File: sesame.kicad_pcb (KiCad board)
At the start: 2 copper layers, 344.4 x 130.9 mm, 166 parts, among them U1 ATmega32A-PU

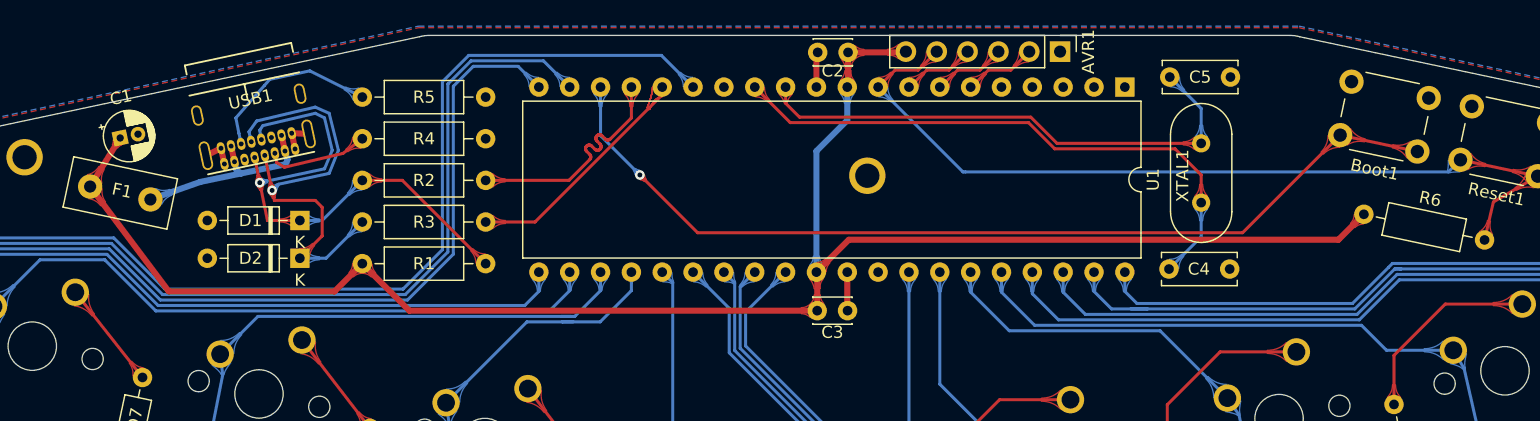
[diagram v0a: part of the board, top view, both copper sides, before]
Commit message: Change to Mini USB
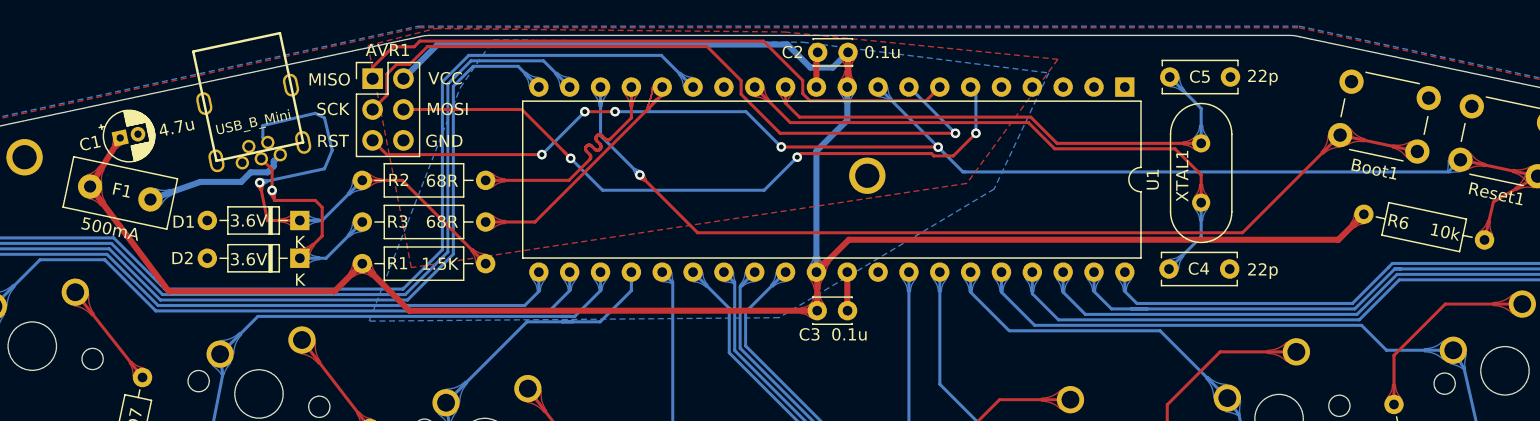
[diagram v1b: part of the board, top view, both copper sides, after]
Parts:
- removed R4, R5: 5.1K, Resistor_THT:R_Axial_DIN0207_L6.3mm_D2.5mm_P10.16mm_Horizontal
- AVR1: value Conn_01x06 -> Conn_02x03_Odd_Even; footprint Connector_PinHeader_2.54mm:PinHeader_1x06_P2.54mm_Vertical -> Connector_PinHeader_2.54mm:PinHeader_2x03_P2.54mm_Vertical
- USB1: value USB_C_Receptacle_USB2.0 -> USB_B_Mini; footprint custom_parts:USB_C_GCT_USB4085 -> Keebio-Parts:USB-Mini-B_ LCSC-C46398
- moved AVR1 56.7 mm to (171.1, 69.1), turned to 0 degrees
- moved USB1 5.71 mm to (161.8, 75.1)
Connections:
- AVR1 pad 1: GND -> MISO
- AVR1 pad 2: MOSI -> +5V
- AVR1 pad 3: MISO -> SCK
- AVR1 pad 4: SCK -> MOSI
- AVR1 pad 6: +5V -> GND
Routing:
- net SCK: track 6.04 -> 60.3 mm, vias 0 -> 1
- net MOSI: track 6.04 -> 56.9 mm, vias 0 -> 3
- net MISO: track 6.04 -> 51.7 mm
- net RST: track 71.2 -> 114.9 mm, vias 0 -> 5
- net +5V: track 145.7 -> 180.0 mm
- net Net-(D2-Pad1): track 37.6 -> 19.3 mm
- net Net-(R5-Pad1): track 14.6 -> 0.00 mm
- net Net-(R4-Pad1): track 8.48 -> 0.00 mm
- net GND: track 11.5 -> 6.09 mm
- net VCC: track 16.5 -> 12.1 mm
- net Net-(D1-Pad1): track 43.8 -> 42.0 mm
